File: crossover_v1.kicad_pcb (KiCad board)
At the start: 2 copper layers, 81 x 47 mm, 39 parts, among them J1 POWER, J2 IN, J3 OUT, J4 OUT, J5 OUT, U1 TL082, U2 TL082

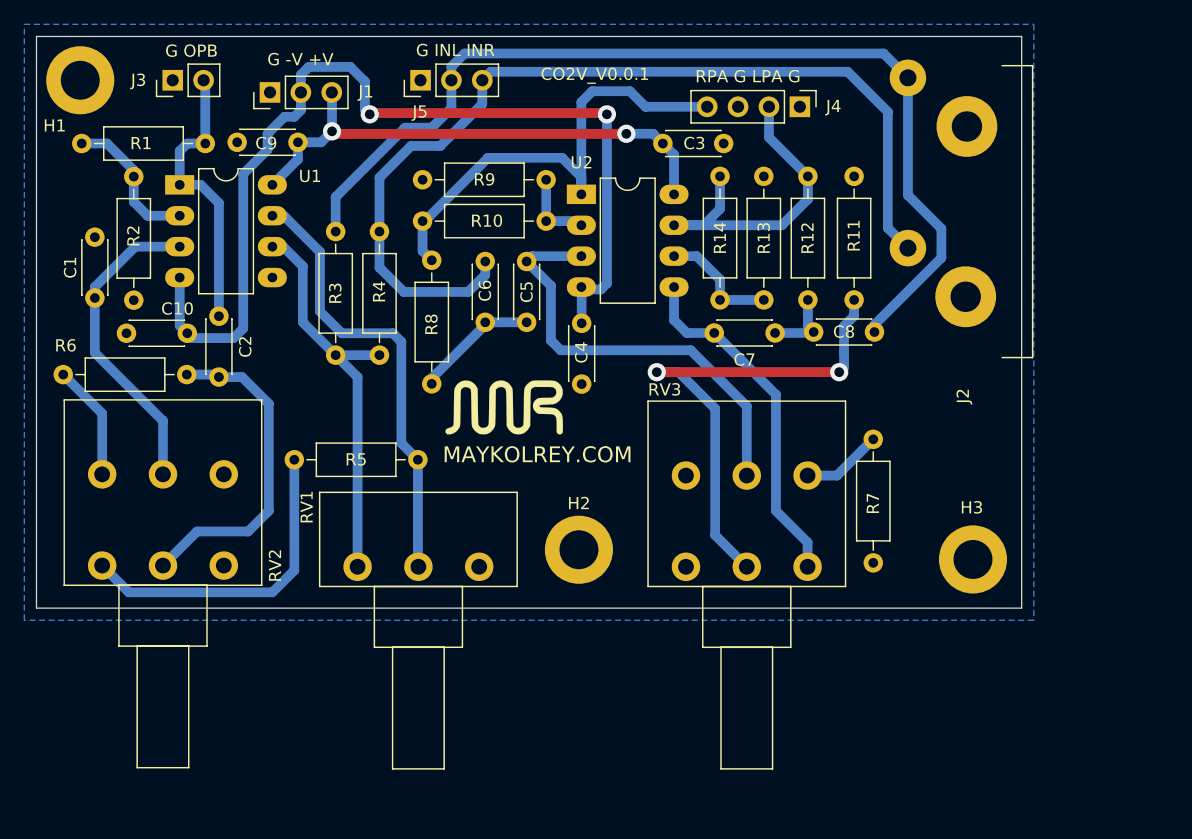
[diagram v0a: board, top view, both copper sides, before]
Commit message: agregando control de volumen de medios, corrigiendo espacio de potenciometro doble
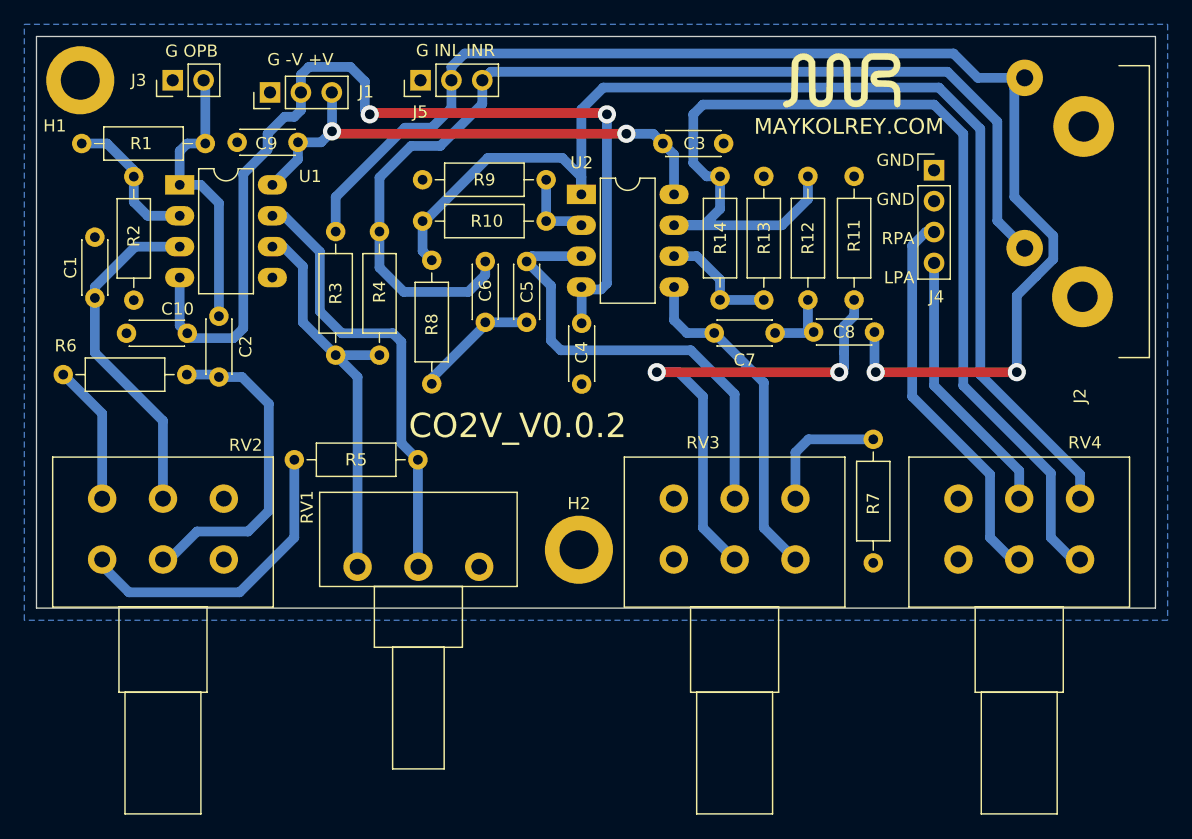
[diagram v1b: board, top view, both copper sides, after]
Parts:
- removed H3: MountingHole, MountingHole:MountingHole_3.2mm_M3_DIN965_Pad
- added RV4: 5K, Potentiometer_THT:Potentiometer_Alps_RK163_Dual_Horizontal, F.Cu at (80.8, 48.0)
- RV2, RV3: footprint Potentiometer_THT:Potentiometer_Piher_T-16H_Double_Horizontal -> Potentiometer_THT:Potentiometer_Alps_RK163_Dual_Horizontal
- moved G*** 38.6 mm to (71.2, 8.60)
- moved J4 12.2 mm to (78.8, 16.0), turned to 0 degrees
- moved J2 9.60 mm to (91.0, 19.4)
- moved RV3 1.17 mm to (57.4, 48.0)
- moved RV2 0.50 mm to (10.4, 48.0)
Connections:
- J4 pad 2: /IZQUIERDO -> GND
- J4 pad 3: GND -> /IZQUIERDO
- R10 pad 1: /DERECHO -> /filtroPasaAltas1/OUT
- R12 pad 1: /IZQUIERDO -> /filtroPasaAltas/OUT
- R14 pad 1: /IZQUIERDO -> /filtroPasaAltas/OUT
- R8 pad 1: /DERECHO -> /filtroPasaAltas1/OUT
- U2 pad 1: /DERECHO -> /filtroPasaAltas1/OUT
- U2 pad 7: /IZQUIERDO -> /filtroPasaAltas/OUT
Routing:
- net /filtroPasaAltas1/OUT: track 0.00 -> 96.5 mm
- net /filtroPasaAltas/OUT: track 0.00 -> 90.5 mm
- net /IN_L: track 81.9 -> 109.3 mm, vias 0 -> 2
- net /DERECHO: track 39.6 -> 22.3 mm
- net /IN_R: track 78.4 -> 87.2 mm
- net /IZQUIERDO: track 27.8 -> 32.3 mm
- net /filtroPasaAltas1/POT_N: track 6.63 -> 10.6 mm
- net Net-(R6-Pad1): track 9.53 -> 11.5 mm
- net Net-(C1-Pad2): track 26.1 -> 28.1 mm
- net Net-(R5-Pad1): track 26.6 -> 25.0 mm
- net /filtroPasaAltas1/POT_P: track 36.0 -> 37.5 mm
- net /filtroPasaAltas/POT_N: track 41.6 -> 40.6 mm
- net /filtroPasaAltas/POT_P: track 28.9 -> 27.8 mm
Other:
- board size 81 x 47 mm -> 92 x 47 mm
- board text added: "CO2V_V0.0.2"
- board text added: "GND GND RPA LPA"
- board text removed: "CO2V_V0.0.1"
- board text removed: "RPA G LPA G"

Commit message: agregando archivos pdf
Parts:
- moved C10 120.5 mm to (113.8, 101.8)
- moved C2 120.5 mm to (116.4, 100.4)
- moved C3 120.5 mm to (157.9, 86.2)
- moved C6 120.5 mm to (138.3, 100.9)
- moved C7 120.5 mm to (157.1, 101.8)
- moved C8 120.5 mm to (165.3, 101.7)
- moved J1 120.5 mm to (120.6, 82.0)
- moved J2 120.5 mm to (187.4, 91.8)
- moved J3 120.5 mm to (112.6, 81.0)
- moved R10 120.5 mm to (133.1, 92.5)
- moved R11 120.5 mm to (168.6, 99.0)
- moved R2 120.5 mm to (109.4, 88.9)
- moved R5 120.5 mm to (122.6, 112.2)
- moved R6 120.5 mm to (103.6, 105.2)
- moved R8 120.5 mm to (133.9, 95.8)
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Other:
- board text added: "Crossover ${REVISION}"
- board text removed: "CO2V_V0.0.2"
